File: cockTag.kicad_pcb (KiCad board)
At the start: 4 copper layers, 25 x 25 mm, 46 parts, among them J1 SWD, Q1 Q_NPN_BEC, U1 KXTJ3-1057, U2 nRF51x22-QFxx, Y1 32.768kHz, Y2 16MHz

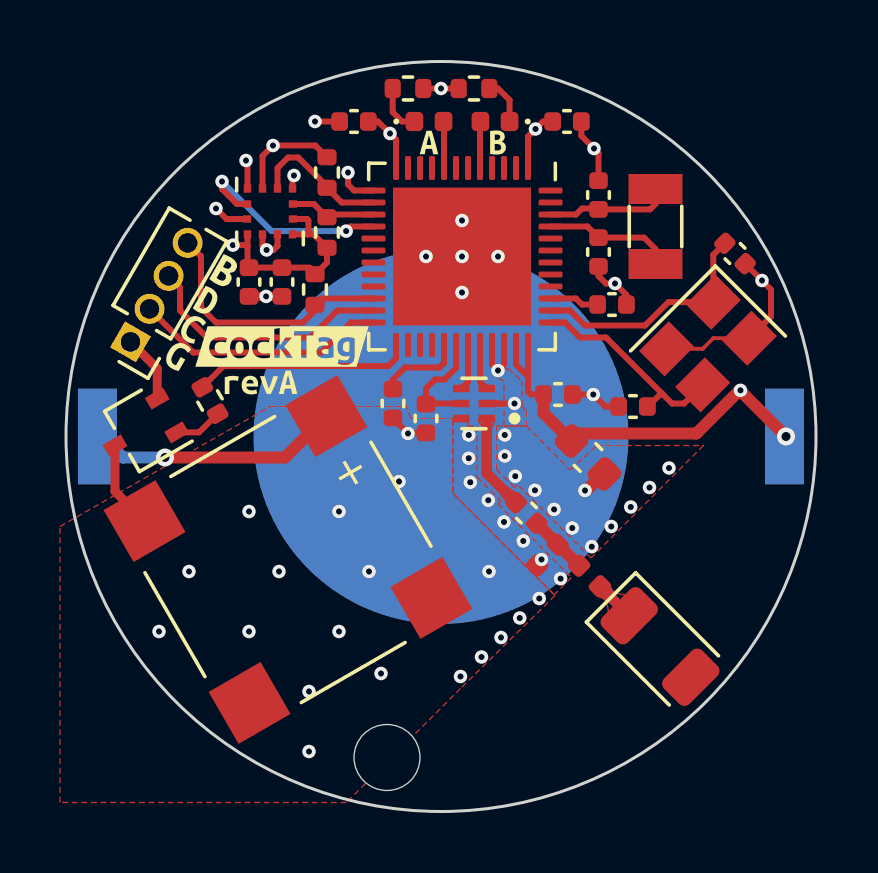
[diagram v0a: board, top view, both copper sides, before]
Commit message: Minor PCB layout fix
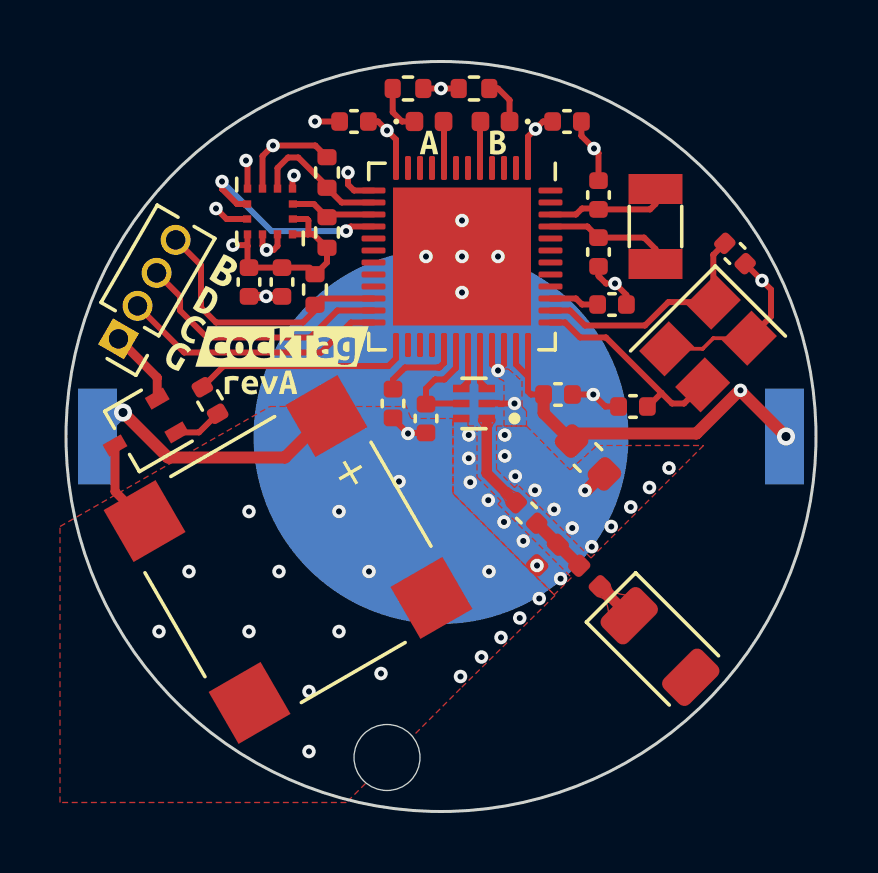
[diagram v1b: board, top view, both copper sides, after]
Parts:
- moved J1 0.41 mm to (139.4, 96.7)
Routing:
- net VCC: track 36.5 -> 37.5 mm
